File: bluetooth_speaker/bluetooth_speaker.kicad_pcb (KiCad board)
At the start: 2 copper layers, 5 parts, among them U1 MAX98357A, U2 XL4015, U3 ESP32-WROOM-32UE, U4 ESP32-D0WD-V3

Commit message: Updated schematic
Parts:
- added J2: USB_C_Receptacle_USB2.0_16P, Connector_USB:USB_C_Receptacle_GCT_USB4085, F.Cu at (120.0, 78.0)
- added U5: 282836-4, 282836-4:282836-4_TYC, F.Cu at (110.0, 94.5)
- added Y1: 40MHz(±10 ppm), Crystal:Crystal_SMD_SeikoEpson_MC306-4Pin_8.0x3.2mm, F.Cu at (141.5, 81.0)
- U3: value ESP32-WROOM-32UE -> CP2102N-A01-GQFN28; footprint RF_Module:ESP32-WROOM-32UE -> CP2102N-A01-GQFN28:QFN28_5X5_SIL
- moved U2 42.6 mm to (138.3, 58.0)
- moved U1 33.2 mm to (141.7, 70.3)
- moved U3 29.4 mm to (112.5, 80.0)
- moved U4 26.8 mm to (133.0, 71.5)
- moved D2 21.5 mm to (119.3, 72.1)
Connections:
- U1 pad 1: DATA -> /DATA
- U1 pad 10: Net-(U1-OUTN) -> /Audio/AUDIO_OUT-
- U1 pad 14: LRCLK -> /LRCLK
- U1 pad 16: BLCK -> /BCLK
- U1 pad 2: +3.3V -> unconnected-(U1-GAIN_SLOT-Pad2)
- U1 pad 9: Net-(U1-OUTP) -> /Audio/AUDIO_OUT+
- U2 pad 5: +BATT -> /Power/Batt+
- U3 pad 10: LRCLK -> unconnected-(U3-NC-Pad10)
- U3 pad 11: DATA -> unconnected-(U3-SUSPENDb-Pad11)
- U3 pad 2: +3.3V -> unconnected-(U3-RI/CLK-Pad2)
- U3 pad 25: SD_MODE -> /U0RXD
- U3 pad 26: unconnected-(U3-IO4-Pad26) -> /U0TXD
- U3 pad 27: Vdd33 -> unconnected-(U3-DSR-Pad27)
- U3 pad 29: unconnected-(U3-IO5-Pad29) -> GND
- U3 pad 3: unconnected-(U3-EN-Pad3) -> GND
- U3 pad 4: unconnected-(U3-SENSOR_VP-Pad4) -> /USB-UART Converter/USB_D+
- U3 pad 5: unconnected-(U3-SENSOR_VN-Pad5) -> /USB-UART Converter/USB_D-
- U3 pad 6: unconnected-(U3-IO34-Pad6) -> +3.3V
- U3 pad 7: unconnected-(U3-IO35-Pad7) -> +3.3V
- U3 pad 8: unconnected-(U3-IO32-Pad8) -> Net-(U3-VBUS)
- U3 pad 9: unconnected-(U3-IO33-Pad9) -> Net-(U3-RSTb)
- U4 pad 14: unconnected-(U4-GPIO25-Pad14) -> /LRCLK
- U4 pad 15: unconnected-(U4-GPIO26-Pad15) -> /BCLK
- U4 pad 16: unconnected-(U4-GPIO27-Pad16) -> /SD_MODE
- U4 pad 19: unconnected-(U4-VDD3P3_RTC-Pad19) -> +3.3V
- U4 pad 26: unconnected-(U4-VDD_SDIO-Pad26) -> +3.3V
- U4 pad 37: unconnected-(U4-VDD3P3_CPU-Pad37) -> +3.3V
- U4 pad 39: unconnected-(U4-GPIO22-Pad39) -> /DATA
- U4 pad 40: unconnected-(U4-U0RXD-Pad40) -> /U0RXD
- U4 pad 41: unconnected-(U4-U0TXD-Pad41) -> /U0TXD
- U4 pad 43: unconnected-(U4-VDDA-Pad43) -> +3.3V
- U4 pad 44: unconnected-(U4-XTAL_N-Pad44) -> /XTAL_N
- U4 pad 45: unconnected-(U4-XTAL_P-Pad45) -> /XTAL_P
- U4 pad 46: unconnected-(U4-VDDA-Pad46) -> +3.3V

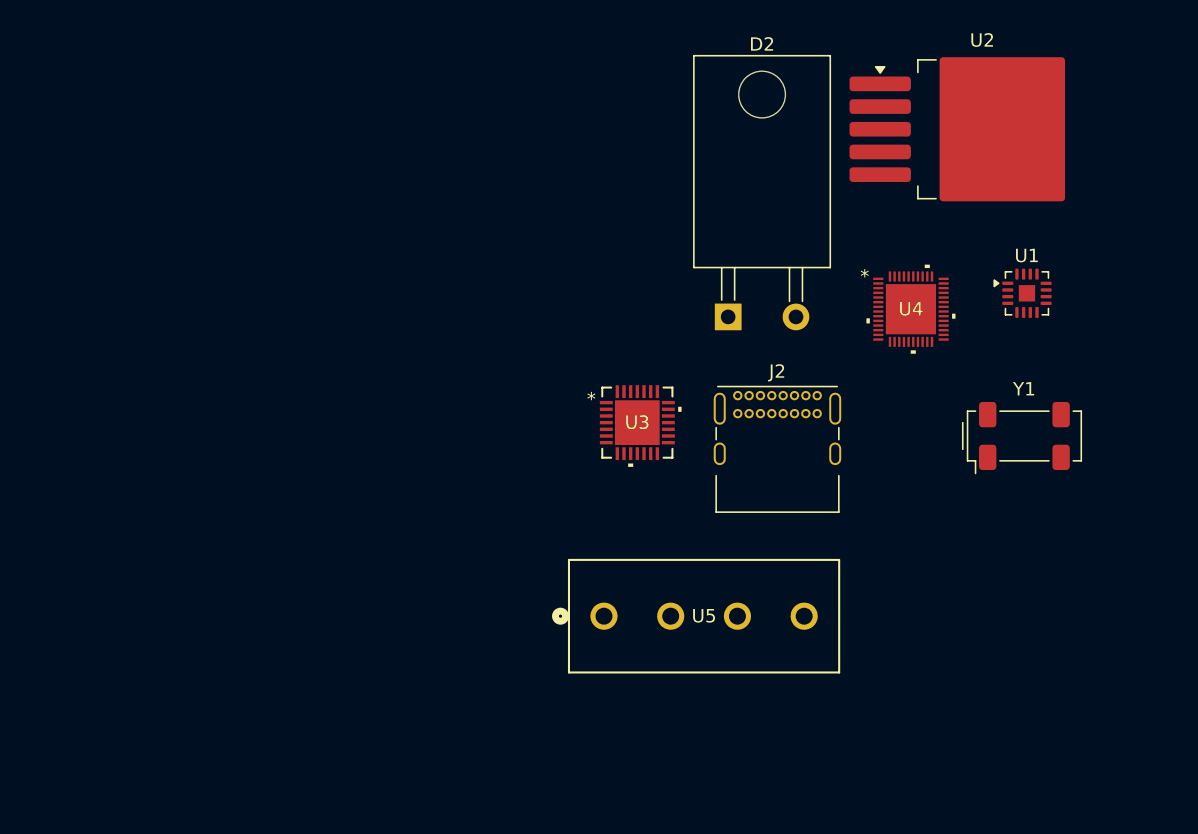
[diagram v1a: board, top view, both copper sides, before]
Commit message: Completed adding footprints, set up PCB rules
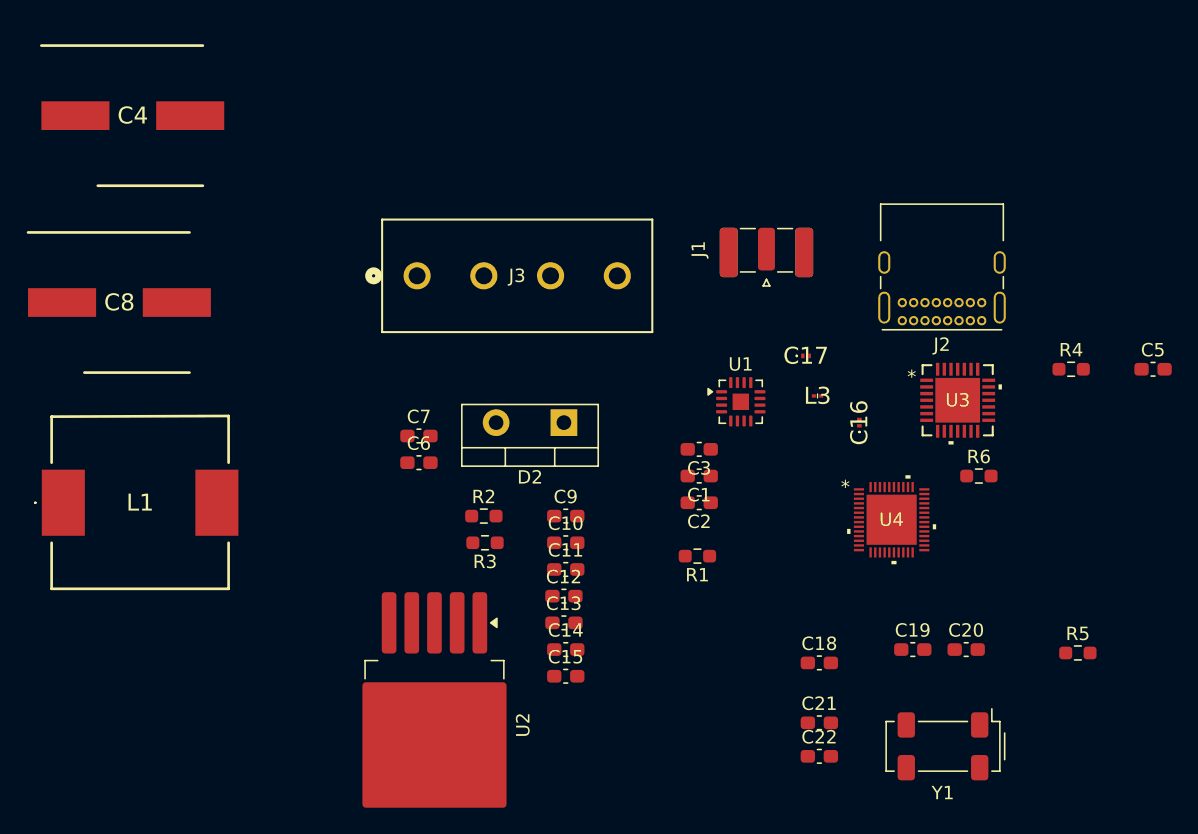
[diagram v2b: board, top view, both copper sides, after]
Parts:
- removed U5: 282836-4, 282836-4:282836-4_TYC
- added C1: 10µF, Capacitor_SMD:C_0603_1608Metric_Pad1.08x0.95mm_HandSolder, F.Cu at (117.1, 84.0)
- added C10: 0.1µF, Capacitor_SMD:C_0603_1608Metric_Pad1.08x0.95mm_HandSolder, F.Cu at (107.1, 89.0)
- added C11: 100pF, Capacitor_SMD:C_0603_1608Metric_Pad1.08x0.95mm_HandSolder, F.Cu at (107.1, 91.0)
- added C12: 0.1µF, Capacitor_SMD:C_0603_1608Metric_Pad1.08x0.95mm_HandSolder, F.Cu at (107.0, 93.0)
- added C13: 10µF, Capacitor_SMD:C_0603_1608Metric_Pad1.08x0.95mm_HandSolder, F.Cu at (107.0, 95.0)
- added C14: 1µF, Capacitor_SMD:C_0603_1608Metric_Pad1.08x0.95mm_HandSolder, F.Cu at (107.1, 97.0)
- added C15: 0.1µF, Capacitor_SMD:C_0603_1608Metric_Pad1.08x0.95mm_HandSolder, F.Cu at (107.1, 99.0)
- added C16: 1.5pF, SamacSys_Parts:GRM033D70J224ME01D, F.Cu at (129.1, 80.0)
- added C17: 1.5pF, SamacSys_Parts:GRM033D70J224ME01D, F.Cu at (125.1, 75.0)
- added C18: 1µF, Capacitor_SMD:C_0603_1608Metric_Pad1.08x0.95mm_HandSolder, F.Cu at (126.1, 98.0)
- added C19: 10pF, Capacitor_SMD:C_0603_1608Metric_Pad1.08x0.95mm_HandSolder, F.Cu at (133.1, 97.0)
- added C2: 0.1µF, Capacitor_SMD:C_0603_1608Metric_Pad1.08x0.95mm_HandSolder, F.Cu at (117.1, 86.0)
- added C20: 10pF, Capacitor_SMD:C_0603_1608Metric_Pad1.08x0.95mm_HandSolder, F.Cu at (137.1, 97.0)
- added C21: 4.7µF, Capacitor_SMD:C_0603_1608Metric_Pad1.08x0.95mm_HandSolder, F.Cu at (126.1, 102.5)
- added C22: 0.1µF, Capacitor_SMD:C_0603_1608Metric_Pad1.08x0.95mm_HandSolder, F.Cu at (126.1, 105.0)
- added C3: 1µF, Capacitor_SMD:C_0603_1608Metric_Pad1.08x0.95mm_HandSolder, F.Cu at (117.1, 82.0)
- added C4: 330µF/25V, SamacSys_Parts:CAPAE1050X1250N, F.Cu at (74.7, 57.0)
- added C5: 0.1µF, Capacitor_SMD:C_0603_1608Metric_Pad1.08x0.95mm_HandSolder, F.Cu at (151.1, 76.0)
- added C6: 1µF, Capacitor_SMD:C_0603_1608Metric_Pad1.08x0.95mm_HandSolder, F.Cu at (96.1, 83.0)
- added C7: 1µF, Capacitor_SMD:C_0603_1608Metric_Pad1.08x0.95mm_HandSolder, F.Cu at (96.1, 81.0)
- added C8: 220µF/50V, SamacSys_Parts:CAPAE1050X1250N, F.Cu at (73.7, 71.0)
- added C9: 1µF, Capacitor_SMD:C_0603_1608Metric_Pad1.08x0.95mm_HandSolder, F.Cu at (107.1, 87.0)
- added J1: Conn_Coaxial, Connector_Coaxial:SMA_Samtec_SMA-J-P-H-ST-EM1_EdgeMount, F.Cu at (122.2, 67.0)
- added J3: 282836-4, 282836-4:282836-4_TYC, F.Cu at (96.0, 69.0)
- added L1: 47µH/5A, SamacSys_Parts:IHLP5050FDER470M5A, F.Cu at (75.2, 86.0)
- added L3: 2.7nH, SamacSys_Parts:LQP03TG3N1B02D, F.Cu at (126.0, 78.0)
- added R1: 300kΩ, Resistor_SMD:R_0603_1608Metric_Pad0.98x0.95mm_HandSolder, F.Cu at (117.0, 90.0)
- added R2: 16.5kΩ, Resistor_SMD:R_0603_1608Metric_Pad0.98x0.95mm_HandSolder, F.Cu at (101.0, 87.0)
- added R3: 10kΩ, Resistor_SMD:R_0603_1608Metric_Pad0.98x0.95mm_HandSolder, F.Cu at (101.1, 89.0)
- added R4: 22.1kΩ, Resistor_SMD:R_0603_1608Metric_Pad0.98x0.95mm_HandSolder, F.Cu at (145.0, 76.0)
- added R5: 47.5kΩ, Resistor_SMD:R_0603_1608Metric_Pad0.98x0.95mm_HandSolder, F.Cu at (145.5, 97.3)
- added R6: 1kΩ, Resistor_SMD:R_0603_1608Metric_Pad0.98x0.95mm_HandSolder, F.Cu at (138.1, 84.0)
- D2: footprint Package_TO_SOT_THT:TO-220-2_Horizontal_TabDown -> Package_TO_SOT_THT:TO-220-2_Vertical
- moved U2 60.6 mm to (97.3, 102.7), turned to -90 degrees
- moved U3 24.1 mm to (136.5, 78.3)
- moved Y1 24.0 mm to (135.4, 104.2), turned to 180 degrees
- moved U1 22.9 mm to (120.2, 78.4)
- moved J2 19.1 mm to (138.3, 72.4), turned to 180 degrees
- moved U4 15.8 mm to (131.6, 87.3)
- moved D2 14.6 mm to (107.0, 80.0), turned to 180 degrees
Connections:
- U1 pad 17: unconnected-(U1-PAD-Pad17) -> GND
- U3 pad 25: /U0RXD -> /U0TXD
- U3 pad 26: /U0TXD -> /U0RXD
- U4 pad 3: Net-(L2-Pad2) -> +3.3V
- U4 pad 4: Net-(L2-Pad2) -> +3.3V
- Y1 pad 1: Net-(C20-Pad2) -> /XTAL_P

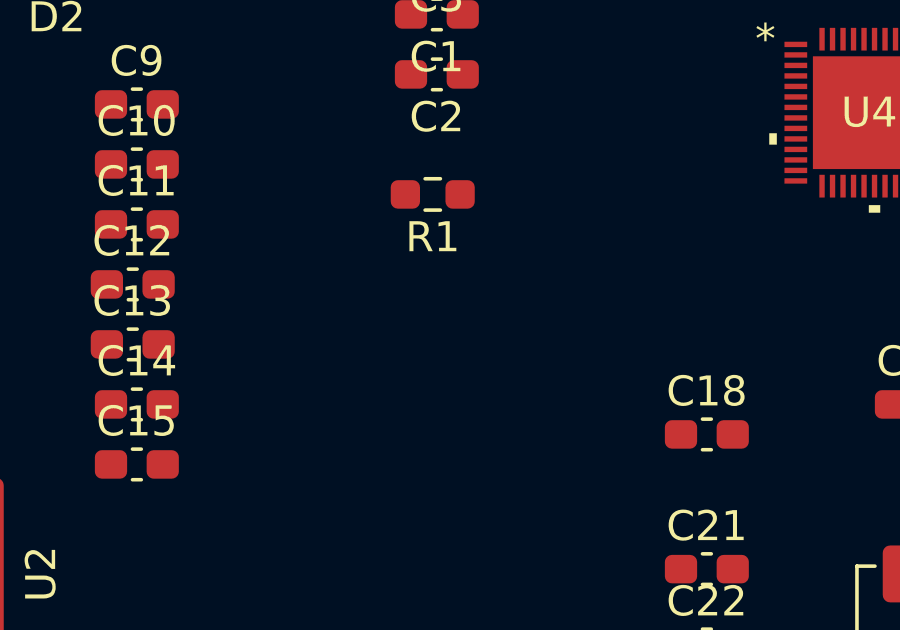
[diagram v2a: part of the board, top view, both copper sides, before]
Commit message: Added missing inductor
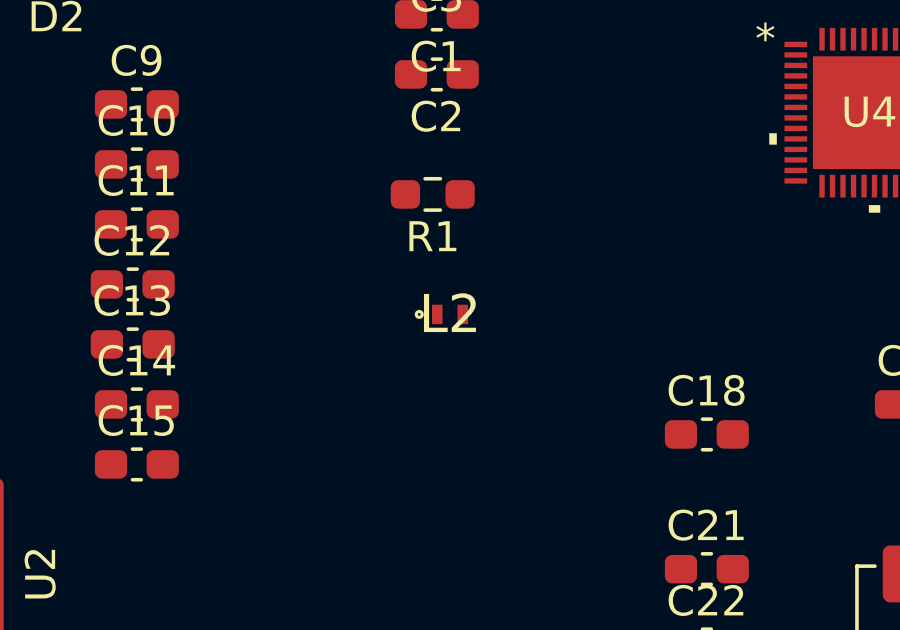
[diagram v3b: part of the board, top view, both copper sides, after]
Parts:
- added L2: 2nH, SamacSys_Parts:MHQ1005, F.Cu at (117.6, 94.0)
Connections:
- U4 pad 3: +3.3V -> Net-(L2-Pad2)
- U4 pad 4: +3.3V -> Net-(L2-Pad2)
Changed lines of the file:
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@@
 	(net 82 "unconnected-(U3-GPIO.2{slash}RS485-Pad17)")
 	(net 83 "unconnected-(U3-GPIO.6-Pad20)")
+	(net 84 "Net-(L2-Pad2)")
 	(footprint "Resistor_SMD:R_0603_1608Metric_Pad0.98x0.95mm_HandSolder"
 		(layer "F.Cu")
@@
 			)
 		)
-		(property "Datasheet" "~"
+		(property "Datasheet" "https://www.mouser.pl/ProductDetail/Taoglas/EMPCB.SMAFSTJ.C.HT?qs=AL7xPqYNrmS49k5WLHoXWA%3D%3D"
 			(at 0 0 180)
 			(unlocked yes)
@@
 		)
 	)
+	(footprint "SamacSys_Parts:MHQ1005"
+		(layer "F.Cu")
+		(at 117.575 94)
+		(descr "MHQ1005")
+		(tags "Inductor")
+		(property "Reference" "L2"
+			(at 0 0 0)
+			(layer "F.SilkS")
+			(effects
+				(font
+					(size 1.27 1.27)
+					(thickness 0.254)
+				)
+			)
+		)
+		(property "Value" "2nH"
+			(at 0 0 0)
+			(layer "F.SilkS")
+			(hide yes)
+			(effects
+				(font
+					(size 1.27 1.27)
+					(thickness 0.254)
+				)
+			)
+		)
+		(property "Datasheet" "https://www.mouser.pl/ProductDetail/TDK/MHQ1005P2N0BTD25?qs=sGAEpiMZZMv126LJFLh8y5lwrxezZJ61ff3nV176I9k%3D"
+			(at 0 0 0)
+			(layer "F.Fab")
+			(hide yes)
+			(effects
+				(font
+					(size 1.27 1.27)
+					(thickness 0.15)
+				)
+			)
+		)
+		(property "Description" "Inductor"
+			(at 0 0 0)
+			(layer "F.Fab")
+			(hide yes)
+			(effects
+				(font
+					(size 1.27 1.27)
+					(thickness 0.15)
+				)
+			)
+		)
+		(property ki_fp_filters "Choke_* *Coil* Inductor_* L_*")
+		(sheetname "/")
+		(sheetfile "bluetooth_speaker.kicad_sch")
+		(attr smd)
+		(fp_circle
+			(center -1.025 0)
+			(end -1.025 0.05)
+			(stroke
+				(width 0.2)
+				(type solid)
+			)
+			(fill no)
+			(layer "F.SilkS")
+		)
+		(fp_line
+			(start -1.625 -1)
+			(end 1.2 -1)
+			(stroke
+				(width 0.05)
+				(type solid)
+			)
+			(layer "F.CrtYd")
+		)
+		(fp_line
+			(start -1.625 1)
+			(end -1.625 -1)
+			(stroke
+				(width 0.05)
+				(type solid)
+			)
+			(layer "F.CrtYd")
+		)
+		(fp_line
+			(start 1.2 -1)
+			(end 1.2 1)
+			(stroke
+				(width 0.05)
+				(type solid)
+			)
+			(layer "F.CrtYd")
+		)
+		(fp_line
+			(start 1.2 1)
+			(end -1.625 1)
+			(stroke
+				(width 0.05)
+				(type solid)
+			)
+			(layer "F.CrtYd")
+		)
+		(fp_line
+			(start -0.5 -0.3)
+			(end 0.5 -0.3)
+			(stroke
+				(width 0.2)
+				(type solid)
+			)
+			(layer "F.Fab")
+		)
+		(fp_line
+			(start -0.5 0.3)
+			(end -0.5 -0.3)
+			(stroke
+				(width 0.2)
+				(type solid)
+			)
+			(layer "F.Fab")
+		)
+		(fp_line
+			(start 0.5 -0.3)
+			(end 0.5 0.3)
+			(stroke
+				(width 0.2)
+				(type solid)
+			)
+			(layer "F.Fab")
+		)
+		(fp_line
+			(start 0.5 0.3)
+			(end -0.5 0.3)
+			(stroke
+				(width 0.2)
+				(type solid)
+			)
+			(layer "F.Fab")
+		)
+		(fp_text user "${REFERENCE}"
+			(at 0 0 0)
+			(layer "F.Fab")
+			(effects
+				(font
+					(size 1.27 1.27)
+					(thickness 0.254)
+				)
+			)
+		)
+		(pad "1" smd rect
+			(at -0.425 0)
+			(size 0.35 0.65)
+			(layers "F.Cu" "F.Mask" "F.Paste")
+			(net 8 "+3.3V")
+			(pinfunction "1")
+			(pintype "passive")
+		)
+		(pad "2" smd rect
+			(at 0.425 0)
+			(size 0.35 0.65)
+			(layers "F.Cu" "F.Mask" "F.Paste")
+			(net 84 "Net-(L2-Pad2)")
+			(pinfunction "2")
+			(pintype "passive")
+		)
+		(embedded_fonts no)
+		(model "D:\\SamacSys_PCB_Library\\KiCad\\SamacSys_Parts.3dshapes\\MHQ1005P2N0BTD25.stp"
+			(offset
+				(xyz 0 0 0.2499999962)
+			)
+			(scale
+				(xyz 1 1 1)
+			)
+			(rotate
+				(xyz -90 0 0)
+			)
+		)
+	)
 	(footprint "Capacitor_SMD:C_0603_1608Metric_Pad1.08x0.95mm_HandSolder"
 		(layer "F.Cu")
@@
 			(size 0.1786 0.757199)
 			(layers "F.Cu" "F.Mask" "F.Paste")
-			(net 8 "+3.3V")
+			(net 84 "Net-(L2-Pad2)")
 			(pinfunction "VDD3P3")
 			(pintype "power_in")
@@
 			(size 0.1786 0.757199)
 			(layers "F.Cu" "F.Mask" "F.Paste")
-			(net 8 "+3.3V")
+			(net 84 "Net-(L2-Pad2)")
 			(pinfunction "VDD3P3")
 			(pintype "power_in")

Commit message: pcb layout
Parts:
- moved U2 65.6 mm to (119.2, 40.9), turned to 0 degrees
- moved L1 65.3 mm to (134.0, 57.6), turned to 180 degrees
- moved R3 57.3 mm to (96.2, 31.9), turned to 0 degrees
- moved C3 56.8 mm to (80.2, 38.9), turned to 0 degrees
- moved R2 53.3 mm to (96.3, 33.9), turned to 180 degrees
- moved C6 45.4 mm to (101.2, 37.9), turned to 180 degrees
- moved J1 44.4 mm to (125.2, 111.3), turned to -90 degrees
- moved C7 41.4 mm to (101.2, 39.9), turned to 180 degrees
- moved C4 40.3 mm to (115.0, 57.1), turned to 180 degrees
- moved D2 37.9 mm to (92.0, 45.2)
- moved C17 32.8 mm to (124.0, 107.8)
- moved C16 31.0 mm to (120.5, 109.8), turned to -90 degrees
- moved U1 31.0 mm to (98.5, 100.4)
- moved L3 29.7 mm to (120.7, 107.2)
- moved C9 28.7 mm to (133.7, 97.8), turned to 180 degrees
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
